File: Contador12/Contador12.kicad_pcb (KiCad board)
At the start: 2 copper layers, 43.2 x 38.8 mm, 17 parts, among them J1 Conector_ESP

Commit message: Correcciones Adrian
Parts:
- moved C_F1 90.8 mm to (105.5, 98.0)
- moved ESP12E 90.8 mm to (109.8, 82.8)
- moved J1 90.8 mm to (121.0, 104.8)
- moved LED 90.8 mm to (130.7, 104.5)
- moved MH1 90.8 mm to (103.0, 75.5)
- moved MH2 90.8 mm to (138.8, 75.8)
- moved MH3 90.8 mm to (103.0, 107.0)
- moved MH4 90.8 mm to (138.8, 107.0)
- moved Program1 90.8 mm to (130.8, 85.2)
- moved R_CH1 90.8 mm to (104.0, 86.8)
- moved R_DOWN15 90.8 mm to (130.7, 94.8)
- moved R_DOWN4 90.8 mm to (130.7, 88.8)
- moved R_Program1 90.8 mm to (130.7, 96.8)
- moved R_RST1 90.8 mm to (104.0, 82.8)
- moved R_UP0 90.8 mm to (130.7, 90.8)
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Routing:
- added copper zone on B.Cu, net +3V3
- removed copper zone on B.Cu, net GND
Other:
- board text added: "Margen: 0.25 mm Ancho pista: 0.25 mm Diametro Via: 1 mm Taladro via: 0.4 mm Cuadricula: 0.25 mm Fabricante: https://www.pcbcart.com/pcb-fab/hdi-pcb.html"

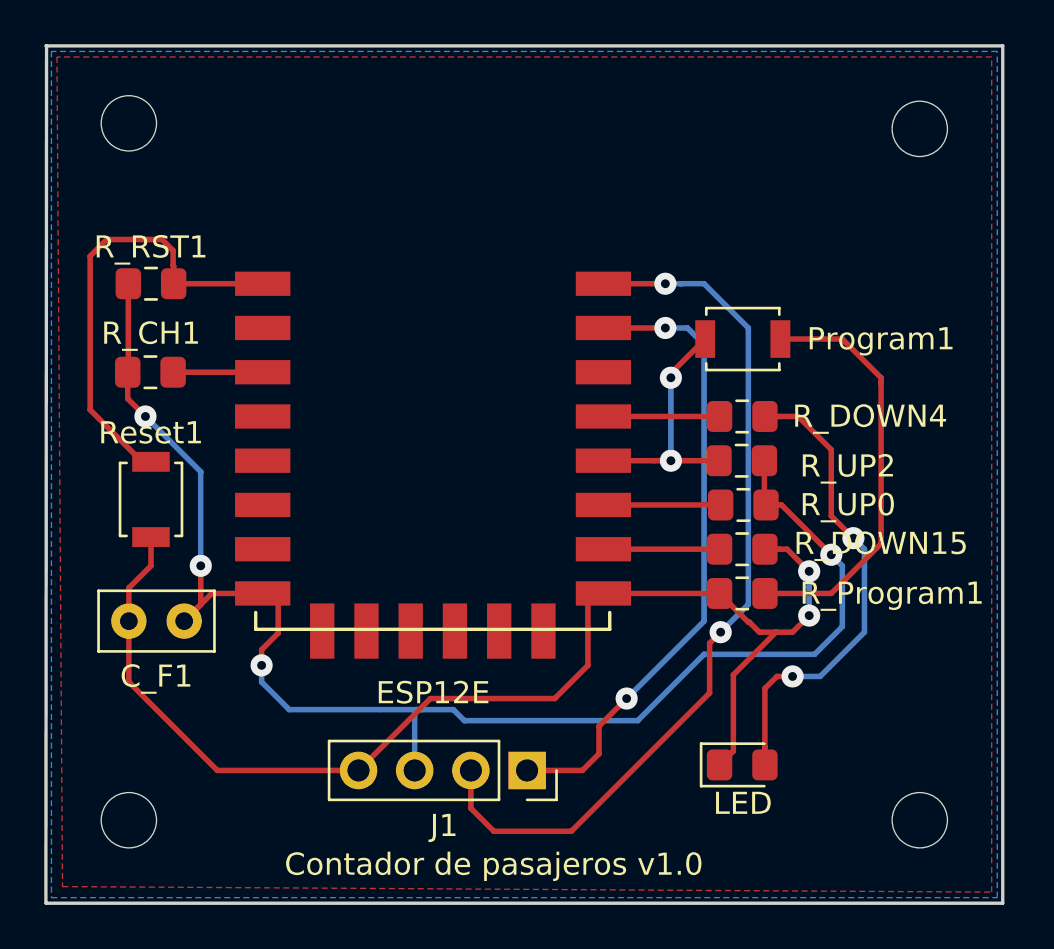
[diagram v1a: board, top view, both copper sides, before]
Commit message: Ajuste de ancho de pistas
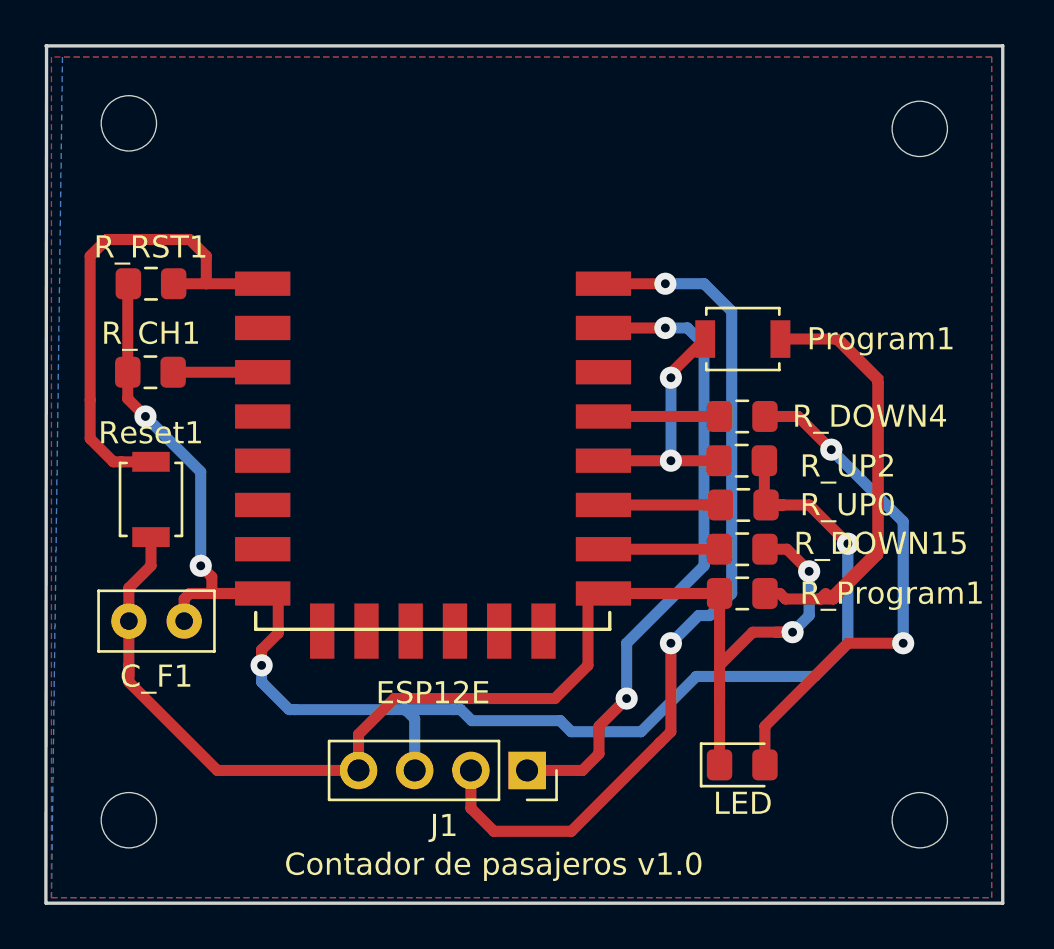
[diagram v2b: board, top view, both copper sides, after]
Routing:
- net Net-(Program1-Pad2): track 19.0 -> 32.7 mm
- net +3V3: track 66.9 -> 79.9 mm
- net GND: track 55.8 -> 68.6 mm
- net Net-(R_UP2-Pad1): track 4.75 -> 10.8 mm
- net Net-(R_DOWN4-Pad1): track 4.70 -> 10.6 mm
- net Net-(R_DOWN15-Pad1): track 4.70 -> 10.6 mm
- net Net-(Program1-Pad1): track 12.1 -> 18.0 mm
- net Net-(R_RST1-Pad2): track 21.2 -> 23.7 mm
- net Net-(D_4-Pad2): track 21.5 -> 23.3 mm
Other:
- net class Default: clearance 0.25 -> 0.5; trace_width 0.25 -> 0.5
- rule trace_clearance: 0.25 -> 0.5
- board text added: "Margen: 0.5 mm Ancho pista: 0.5 mm Diametro Via: 1 mm Taladro via: 0.4 mm Cuadricula: 0.25 mm Fabricante: https://www.pcbcart.com/pcb-fab/hdi-pcb.html"
- board text removed: "Margen: 0.25 mm Ancho pista: 0.25 mm Diametro Via: 1 mm Taladro via: 0.4 mm Cuadricula: 0.25 mm Fabricante: https://www.pcbcart.com/pcb-fab/hdi-pcb.html"
